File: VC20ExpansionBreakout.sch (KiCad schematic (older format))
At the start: 10 parts, among them J1 Other, J2 Power, J3 GND, J4 Breakout, J5 NC, SW1 Reset, U1 VC20-Exp-Port, U2 27C512/27C020

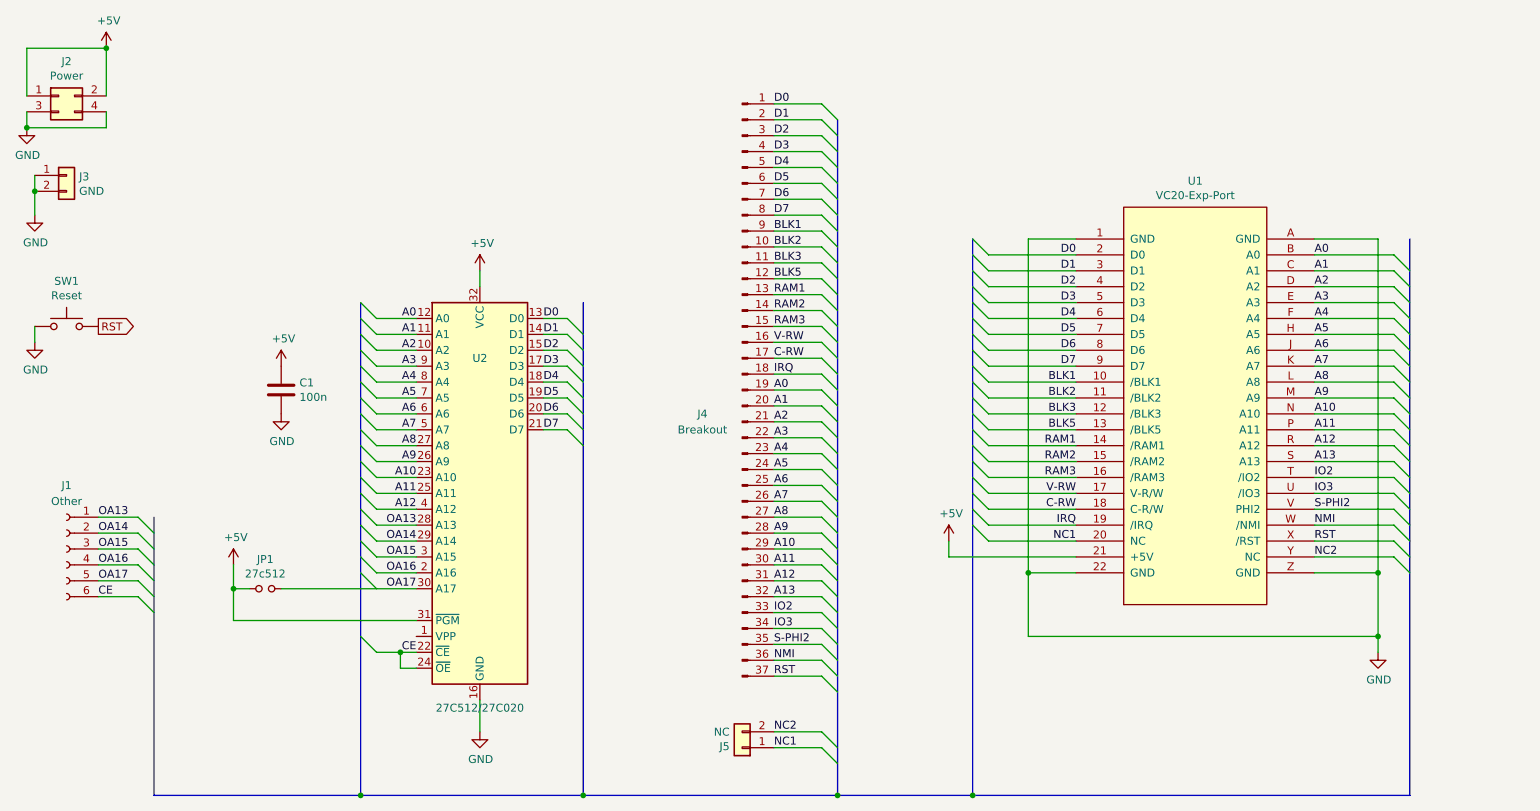
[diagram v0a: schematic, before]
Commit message: Added missing connections.
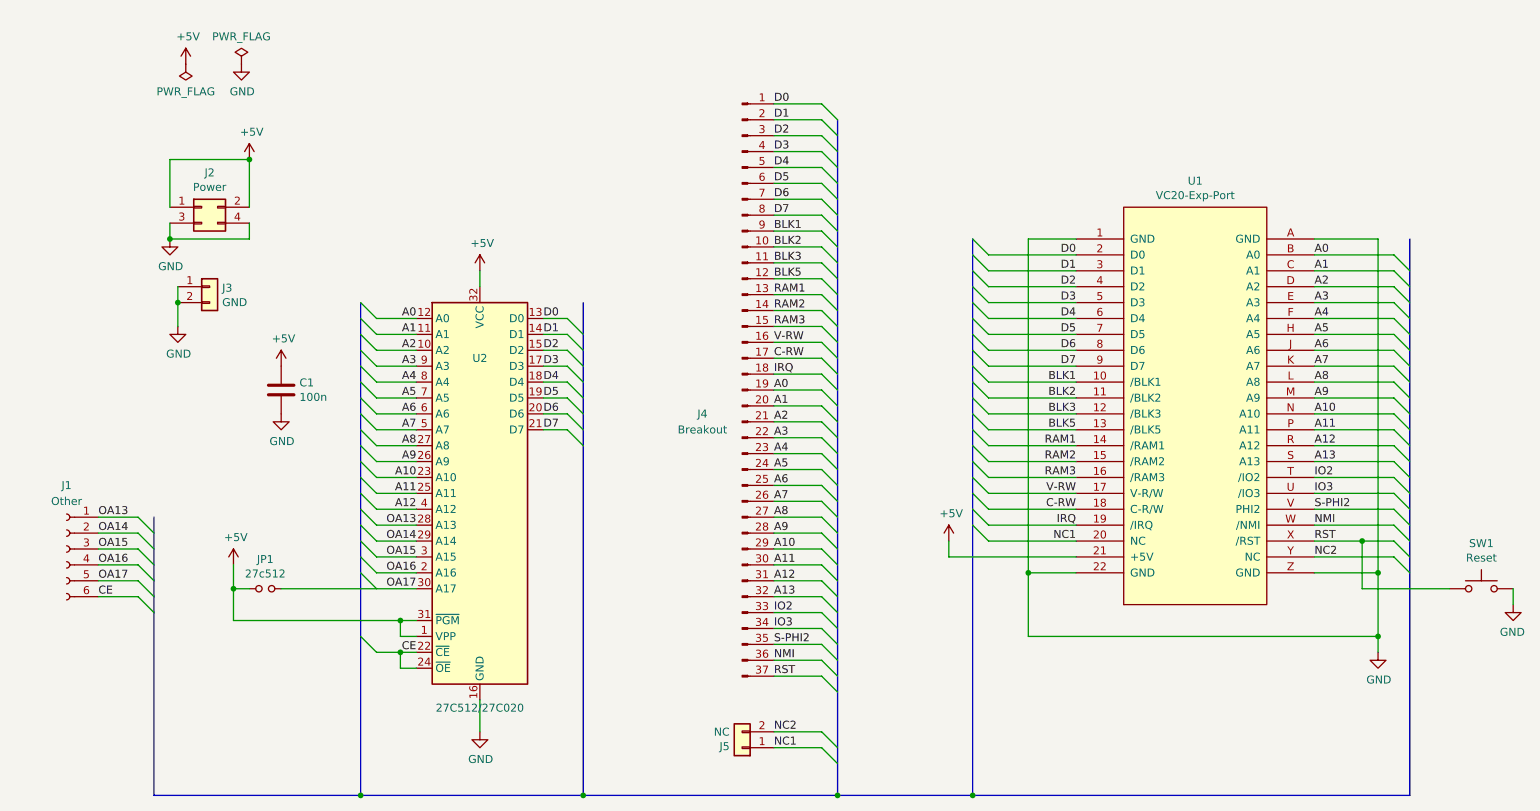
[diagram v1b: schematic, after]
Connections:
- net +5V: now also U2.1 (VPP)
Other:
- moved on the sheet: J2, J3, SW1
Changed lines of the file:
@@
 encoding utf-8
 Sheet 1 1
-Title ""
-Date ""
-Rev ""
-Comp ""
+Title "VC20 Expansion Breakout"
+Date "2020-01-22"
+Rev "1"
+Comp "hackup.net"
 Comment1 ""
 Comment2 ""
@@
 L Connector_Generic:Conn_02x02_Odd_Even J2
 U 1 1 5ACD4D51
-P 1700 1600
-F 0 "J2" H 1750 1817 50  0000 C CNN
-F 1 "Power" H 1750 1726 50  0000 C CNN
-F 2 "Connector_PinHeader_2.54mm:PinHeader_2x02_P2.54mm_Vertical" H 1700 1600 50  0001 C CNN
-F 3 "~" H 1700 1600 50  0001 C CNN
-	1    1700 1600
+P 2600 2300
+F 0 "J2" H 2650 2517 50  0000 C CNN
+F 1 "Power" H 2650 2426 50  0000 C CNN
+F 2 "Connector_PinHeader_2.54mm:PinHeader_2x02_P2.54mm_Vertical" H 2600 2300 50  0001 C CNN
+F 3 "~" H 2600 2300 50  0001 C CNN
+	1    2600 2300
 	1    0    0    -1
 $EndComp
@@
 L Connector_Generic:Conn_01x02 J3
 U 1 1 5ACD5626
-P 1750 2100
-F 0 "J3" H 1829 2092 50  0000 L CNN
-F 1 "GND" H 1829 2001 50  0000 L CNN
-F 2 "Connector_PinHeader_2.54mm:PinHeader_1x02_P2.54mm_Vertical" H 1750 2100 50  0001 C CNN
-F 3 "~" H 1750 2100 50  0001 C CNN
-	1    1750 2100
+P 2650 2800
+F 0 "J3" H 2729 2792 50  0000 L CNN
+F 1 "GND" H 2729 2701 50  0000 L CNN
+F 2 "Connector_PinHeader_2.54mm:PinHeader_1x02_P2.54mm_Vertical" H 2650 2800 50  0001 C CNN
+F 3 "~" H 2650 2800 50  0001 C CNN
+	1    2650 2800
 	1    0    0    -1
 $EndComp
@@
 L Switch:SW_Push SW1
 U 1 1 5ACD57BA
-P 1750 3050
-F 0 "SW1" H 1750 3335 50  0000 C CNN
-F 1 "Reset" H 1750 3244 50  0000 C CNN
-F 2 "Button_Switch_THT:SW_PUSH_6mm" H 1750 3250 50  0001 C CNN
-F 3 "" H 1750 3250 50  0001 C CNN
-	1    1750 3050
-	1    0    0    -1
+P 10650 4700
+F 0 "SW1" H 10650 4985 50  0000 C CNN
+F 1 "Reset" H 10650 4894 50  0000 C CNN
+F 2 "Button_Switch_THT:SW_PUSH_6mm" H 10650 4900 50  0001 C CNN
+F 3 "" H 10650 4900 50  0001 C CNN
+	1    10650 4700
+	-1   0    0    -1
 $EndComp
 $Comp
@@
 L power:GND #PWR0102
 U 1 1 5B8D4EA1
-P 1550 2350
-F 0 "#PWR0102" H 1550 2100 50  0001 C CNN
-F 1 "GND" H 1555 2177 50  0000 C CNN
-F 2 "" H 1550 2350 50  0001 C CNN
-F 3 "" H 1550 2350 50  0001 C CNN
-	1    1550 2350
+P 2450 3050
+F 0 "#PWR0102" H 2450 2800 50  0001 C CNN
+F 1 "GND" H 2455 2877 50  0000 C CNN
+F 2 "" H 2450 3050 50  0001 C CNN
+F 3 "" H 2450 3050 50  0001 C CNN
+	1    2450 3050
 	1    0    0    -1
 $EndComp
@@
 L power:GND #PWR0103
 U 1 1 5B8D5113
-P 1500 1800
-F 0 "#PWR0103" H 1500 1550 50  0001 C CNN
-F 1 "GND" H 1505 1627 50  0000 C CNN
-F 2 "" H 1500 1800 50  0001 C CNN
-F 3 "" H 1500 1800 50  0001 C CNN
-	1    1500 1800
-	1    0    0    -1
-$EndComp
-Wire Wire Line
-	1500 1700 1500 1800
-Wire Wire Line
-	2000 1700 2000 1800
-Wire Wire Line
-	2000 1800 1500 1800
-Connection ~ 1500 1800
+P 2400 2500
+F 0 "#PWR0103" H 2400 2250 50  0001 C CNN
+F 1 "GND" H 2405 2327 50  0000 C CNN
+F 2 "" H 2400 2500 50  0001 C CNN
+F 3 "" H 2400 2500 50  0001 C CNN
+	1    2400 2500
+	1    0    0    -1
+$EndComp
+Wire Wire Line
+	2400 2400 2400 2500
+Wire Wire Line
+	2900 2400 2900 2500
+Wire Wire Line
+	2900 2500 2400 2500
+Connection ~ 2400 2500
 $Comp
 L power:+5V #PWR0104
 U 1 1 5B8D54BC
-P 2000 1300
-F 0 "#PWR0104" H 2000 1150 50  0001 C CNN
-F 1 "+5V" H 2015 1473 50  0000 C CNN
-F 2 "" H 2000 1300 50  0001 C CNN
-F 3 "" H 2000 1300 50  0001 C CNN
-	1    2000 1300
-	1    0    0    -1
-$EndComp
-Wire Wire Line
-	2000 1300 2000 1600
-Wire Wire Line
-	2000 1300 1500 1300
-Wire Wire Line
-	1500 1300 1500 1600
-Connection ~ 2000 1300
+P 2900 2000
+F 0 "#PWR0104" H 2900 1850 50  0001 C CNN
+F 1 "+5V" H 2915 2173 50  0000 C CNN
+F 2 "" H 2900 2000 50  0001 C CNN
+F 3 "" H 2900 2000 50  0001 C CNN
+	1    2900 2000
+	1    0    0    -1
+$EndComp
+Wire Wire Line
+	2900 2000 2900 2300
+Wire Wire Line
+	2900 2000 2400 2000
+Wire Wire Line
+	2400 2000 2400 2300
+Connection ~ 2900 2000
 $Comp
 L power:GND #PWR0105
 U 1 1 5B8D5AE1
-P 1550 3150
-F 0 "#PWR0105" H 1550 2900 50  0001 C CNN
-F 1 "GND" H 1555 2977 50  0000 C CNN
-F 2 "" H 1550 3150 50  0001 C CNN
-F 3 "" H 1550 3150 50  0001 C CNN
-	1    1550 3150
-	1    0    0    -1
-$EndComp
-Wire Wire Line
-	1550 3150 1550 3050
+P 10850 4800
+F 0 "#PWR0105" H 10850 4550 50  0001 C CNN
+F 1 "GND" H 10855 4627 50  0000 C CNN
+F 2 "" H 10850 4800 50  0001 C CNN
+F 3 "" H 10850 4800 50  0001 C CNN
+	1    10850 4800
+	-1   0    0    -1
+$EndComp
+Wire Wire Line
+	10850 4800 10850 4700
 $Comp
 L power:GND #PWR0106
@@
 RST
 Wire Wire Line
-	1550 2200 1550 2350
+	2450 2900 2450 3050
 Wire Wire Line
 	10000 4600 10000 5000
@@
 	9600 4300 10100 4300
 Wire Wire Line
-	9600 4400 10100 4400
-Wire Wire Line
 	9600 4500 10100 4500
 Wire Bus Line
@@
 	4750 3700 4900 3700
 Wire Wire Line
-	2800 4900 3950 4900
+	2800 4900 3850 4900
 Wire Wire Line
 	2800 4700 2800 4900
@@
 Connection ~ 3600 6000
 Wire Wire Line
-	1550 2100 1550 2200
-Connection ~ 1550 2200
+	2450 2800 2450 2900
+Connection ~ 2450 2900
 Wire Wire Line
 	3100 4700 3950 4700
+Wire Wire Line
+	3950 5000 3850 5000
+Wire Wire Line
+	3850 5000 3850 4900
+Connection ~ 3850 4900
+Wire Wire Line
+	3850 4900 3950 4900
+$Comp
+L power:PWR_FLAG #FLG0101
+U 1 1 5E2BABDD
+P 2850 1400
+F 0 "#FLG0101" H 2850 1475 50  0001 C CNN
+F 1 "PWR_FLAG" H 2850 1573 50  0000 C CNN
+F 2 "" H 2850 1400 50  0001 C CNN
+F 3 "~" H 2850 1400 50  0001 C CNN
+	1    2850 1400
+	1    0    0    -1
+$EndComp
+$Comp
+L power:GND #PWR0113
+U 1 1 5E2BC8E8
+P 2850 1400
+F 0 "#PWR0113" H 2850 1150 50  0001 C CNN
+F 1 "GND" H 2855 1227 50  0000 C CNN
+F 2 "" H 2850 1400 50  0001 C CNN
+F 3 "" H 2850 1400 50  0001 C CNN
+	1    2850 1400
+	1    0    0    -1
+$EndComp
+Wire Wire Line
+	9600 4400 9900 4400
+Wire Wire Line
+	9900 4400 9900 4700
+Wire Wire Line
+	9900 4700 10450 4700
+Connection ~ 9900 4400
+Wire Wire Line
+	9900 4400 10100 4400
 Wire Bus Line
 	2300 4250 2300 6000
 Wire Bus Line
+	3600 2900 3600 6000
+Wire Bus Line
 	5000 2900 5000 6000
-Wire Bus Line
-	3600 2900 3600 6000
 Wire Bus Line
 	10200 2500 10200 6000
@@
 Wire Bus Line
 	6600 1750 6600 6000
-Text GLabel 1950 3050 2    50   Output ~ 0
-RST
+$Comp
+L power:+5V #PWR0108
+U 1 1 5E2BC456
+P 2500 1400
+F 0 "#PWR0108" H 2500 1250 50  0001 C CNN
+F 1 "+5V" H 2515 1573 50  0000 C CNN
+F 2 "" H 2500 1400 50  0001 C CNN
+F 3 "" H 2500 1400 50  0001 C CNN
+	1    2500 1400
+	1    0    0    -1
+$EndComp
+$Comp
+L power:PWR_FLAG #FLG0102
+U 1 1 5E2BB50D
+P 2500 1400
+F 0 "#FLG0102" H 2500 1475 50  0001 C CNN
+F 1 "PWR_FLAG" H 2500 1573 50  0000 C CNN
+F 2 "" H 2500 1400 50  0001 C CNN
+F 3 "~" H 2500 1400 50  0001 C CNN
+	1    2500 1400
+	-1   0    0    1
+$EndComp
 $EndSCHEMATC
